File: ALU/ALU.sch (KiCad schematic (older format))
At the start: 40 parts, among them J1 Conn_01x16, J2 Conn_01x16, J3 Conn_01x08, J4 Conn_01x08, U1 74LS86, U10 74LS157, U11 74LS08, U12 74LS157, U13 74LS04, U2 74LS86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

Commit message: Fixed floating inputs; improved power; added parts list; replaced JK latches
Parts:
- added unit 4 of U11
- added unit 2 of U13
- added unit 3 of U13
- added unit 4 of U13
- added unit 5 of U13
- added unit 6 of U13
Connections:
- net GND: now also U13.11, U13.13, U13.3, U13.5, U13.9
- net VCC: now also U11.12, U11.13
- no-connect marks 0 -> 6
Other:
- moved on the sheet: U1E, U2E
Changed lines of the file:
@@
 	2150 5750 2250 5750
 Wire Wire Line
-	1300 7050 1300 7150
-Wire Wire Line
-	1300 5950 1300 6050
-Text GLabel 1300 5950 1    50   Input ~ 0
-VCC
-Text GLabel 1300 7150 3    50   Input ~ 0
+	1500 4950 1500 5050
+Wire Wire Line
+	1500 3850 1500 3950
+Text GLabel 1500 3850 1    50   Input ~ 0
+VCC
+Text GLabel 1500 5050 3    50   Input ~ 0
 GND
 $Comp
 L 74xx:74LS86 U2
 U 5 1 5FAF73A1
-P 1300 6550
-F 0 "U2" H 1530 6596 50  0000 L CNN
-F 1 "74LS86" H 1530 6505 50  0000 L CNN
-F 2 "Package_DIP:DIP-14_W7.62mm" H 1300 6550 50  0001 C CNN
-F 3 "74xx/74ls86.pdf" H 1300 6550 50  0001 C CNN
-	5    1300 6550
+P 1500 4450
+F 0 "U2" H 1650 4950 50  0000 L CNN
+F 1 "74LS86" H 1550 4850 50  0000 L CNN
+F 2 "Package_DIP:DIP-14_W7.62mm" H 1500 4450 50  0001 C CNN
+F 3 "74xx/74ls86.pdf" H 1500 4450 50  0001 C CNN
+	5    1500 4450
 	1    0    0    -1
 $EndComp
@@
 	2150 3250 2250 3250
 Wire Wire Line
-	1300 4500 1300 4600
-Wire Wire Line
-	1300 3400 1300 3500
-Text GLabel 1300 3400 1    50   Input ~ 0
-VCC
-Text GLabel 1300 4600 3    50   Input ~ 0
+	850  4950 850  5050
+Wire Wire Line
+	850  3850 850  3950
+Text GLabel 850  3850 1    50   Input ~ 0
+VCC
+Text GLabel 850  5050 3    50   Input ~ 0
 GND
 $Comp
 L 74xx:74LS86 U1
 U 5 1 5FA507DA
-P 1300 4000
-F 0 "U1" H 1530 4046 50  0000 L CNN
-F 1 "74LS86" H 1530 3955 50  0000 L CNN
-F 2 "Package_DIP:DIP-14_W7.62mm" H 1300 4000 50  0001 C CNN
-F 3 "74xx/74ls86.pdf" H 1300 4000 50  0001 C CNN
-	5    1300 4000
+P 850 4450
+F 0 "U1" H 1000 4950 50  0000 L CNN
+F 1 "74LS86" H 900 4850 50  0000 L CNN
+F 2 "Package_DIP:DIP-14_W7.62mm" H 850 4450 50  0001 C CNN
+F 3 "74xx/74ls86.pdf" H 850 4450 50  0001 C CNN
+	5    850  4450
 	1    0    0    -1
 $EndComp
@@
 Wire Wire Line
 	5200 6700 5200 6800
-Text GLabel 800  2750 1    50   Input ~ 0
+Text GLabel 850  2700 1    50   Input ~ 0
 VCC
 $Comp
 L power:PWR_FLAG #FLG0101
 U 1 1 5FC9E88A
-P 800 2800
-F 0 "#FLG0101" H 800 2875 50  0001 C CNN
-F 1 "PWR_FLAG" H 800 2973 50  0000 C CNN
-F 2 "" H 800 2800 50  0001 C CNN
-F 3 "~" H 800 2800 50  0001 C CNN
-	1    800  2800
+P 850 2750
+F 0 "#FLG0101" H 850 2825 50  0001 C CNN
+F 1 "PWR_FLAG" H 850 2923 50  0000 C CNN
+F 2 "" H 850 2750 50  0001 C CNN
+F 3 "~" H 850 2750 50  0001 C CNN
+	1    850  2750
 	-1   0    0    1
 $EndComp
 Wire Wire Line
-	800  2800 800  2750
-Wire Wire Line
-	800  3300 800  3350
+	850  2750 850  2700
+Wire Wire Line
+	850  3250 850  3300
 $Comp
 L power:PWR_FLAG #FLG0102
 U 1 1 5FCDF7DC
-P 800 3300
-F 0 "#FLG0102" H 800 3375 50  0001 C CNN
-F 1 "PWR_FLAG" H 800 3473 50  0000 C CNN
-F 2 "" H 800 3300 50  0001 C CNN
-F 3 "~" H 800 3300 50  0001 C CNN
-	1    800  3300
-	1    0    0    -1
-$EndComp
-Text GLabel 800  3350 3    50   Input ~ 0
+P 850 3250
+F 0 "#FLG0102" H 850 3325 50  0001 C CNN
+F 1 "PWR_FLAG" H 850 3423 50  0000 C CNN
+F 2 "" H 850 3250 50  0001 C CNN
+F 3 "~" H 850 3250 50  0001 C CNN
+	1    850  3250
+	1    0    0    -1
+$EndComp
+Text GLabel 850  3300 3    50   Input ~ 0
 GND
 $Comp
@@
 Wire Wire Line
 	9950 3350 10300 3350
+$Comp
+L 74xx:74LS04 U13
+U 4 1 60517929
+P 1250 6550
+F 0 "U13" H 1250 6867 50  0000 C CNN
+F 1 "74LS04" H 1250 6776 50  0000 C CNN
+F 2 "Package_DIP:DIP-14_W7.62mm" H 1250 6550 50  0001 C CNN
+F 3 "http://www.ti.com/lit/gpn/sn74LS04" H 1250 6550 50  0001 C CNN
+	4    1250 6550
+	1    0    0    -1
+$EndComp
+$Comp
+L 74xx:74LS04 U13
+U 5 1 6051A436
+P 1250 7050
+F 0 "U13" H 1250 7367 50  0000 C CNN
+F 1 "74LS04" H 1250 7276 50  0000 C CNN
+F 2 "Package_DIP:DIP-14_W7.62mm" H 1250 7050 50  0001 C CNN
+F 3 "http://www.ti.com/lit/gpn/sn74LS04" H 1250 7050 50  0001 C CNN
+	5    1250 7050
+	1    0    0    -1
+$EndComp
+$Comp
+L 74xx:74LS04 U13
+U 6 1 6051C4D5
+P 1250 7550
+F 0 "U13" H 1250 7867 50  0000 C CNN
+F 1 "74LS04" H 1250 7776 50  0000 C CNN
+F 2 "Package_DIP:DIP-14_W7.62mm" H 1250 7550 50  0001 C CNN
+F 3 "http://www.ti.com/lit/gpn/sn74LS04" H 1250 7550 50  0001 C CNN
+	6    1250 7550
+	1    0    0    -1
+$EndComp
+$Comp
+L 74xx:74LS08 U11
+U 4 1 6050CEA2
+P 6350 7100
+F 0 "U11" H 6350 7425 50  0000 C CNN
+F 1 "74LS08" H 6350 7334 50  0000 C CNN
+F 2 "Package_DIP:DIP-14_W7.62mm" H 6350 7100 50  0001 C CNN
+F 3 "http://www.ti.com/lit/gpn/sn74LS08" H 6350 7100 50  0001 C CNN
+	4    6350 7100
+	1    0    0    -1
+$EndComp
+$Comp
+L 74xx:74LS04 U13
+U 3 1 60514840
+P 1250 6050
+F 0 "U13" H 1250 6367 50  0000 C CNN
+F 1 "74LS04" H 1250 6276 50  0000 C CNN
+F 2 "Package_DIP:DIP-14_W7.62mm" H 1250 6050 50  0001 C CNN
+F 3 "http://www.ti.com/lit/gpn/sn74LS04" H 1250 6050 50  0001 C CNN
+	3    1250 6050
+	1    0    0    -1
+$EndComp
+$Comp
+L 74xx:74LS04 U13
+U 2 1 60510F55
+P 1250 5550
+F 0 "U13" H 1250 5867 50  0000 C CNN
+F 1 "74LS04" H 1250 5776 50  0000 C CNN
+F 2 "Package_DIP:DIP-14_W7.62mm" H 1250 5550 50  0001 C CNN
+F 3 "http://www.ti.com/lit/gpn/sn74LS04" H 1250 5550 50  0001 C CNN
+	2    1250 5550
+	1    0    0    -1
+$EndComp
+Text GLabel 850  5550 0    50   Input ~ 0
+GND
+Wire Wire Line
+	850  5550 950  5550
+Text GLabel 850  6050 0    50   Input ~ 0
+GND
+Wire Wire Line
+	850  6050 950  6050
+Text GLabel 850  6550 0    50   Input ~ 0
+GND
+Wire Wire Line
+	850  6550 950  6550
+Text GLabel 850  7050 0    50   Input ~ 0
+GND
+Wire Wire Line
+	850  7050 950  7050
+Text GLabel 850  7550 0    50   Input ~ 0
+GND
+Wire Wire Line
+	850  7550 950  7550
+NoConn ~ 1550 5550
+NoConn ~ 1550 6050
+NoConn ~ 1550 6550
+NoConn ~ 1550 7050
+NoConn ~ 1550 7550
+Text GLabel 5950 7100 0    50   Input ~ 0
+VCC
+Wire Wire Line
+	6050 7000 6050 7100
+Wire Wire Line
+	5950 7100 6050 7100
+Connection ~ 6050 7100
+Wire Wire Line
+	6050 7100 6050 7200
+NoConn ~ 6650 7100
 $EndSCHEMATC

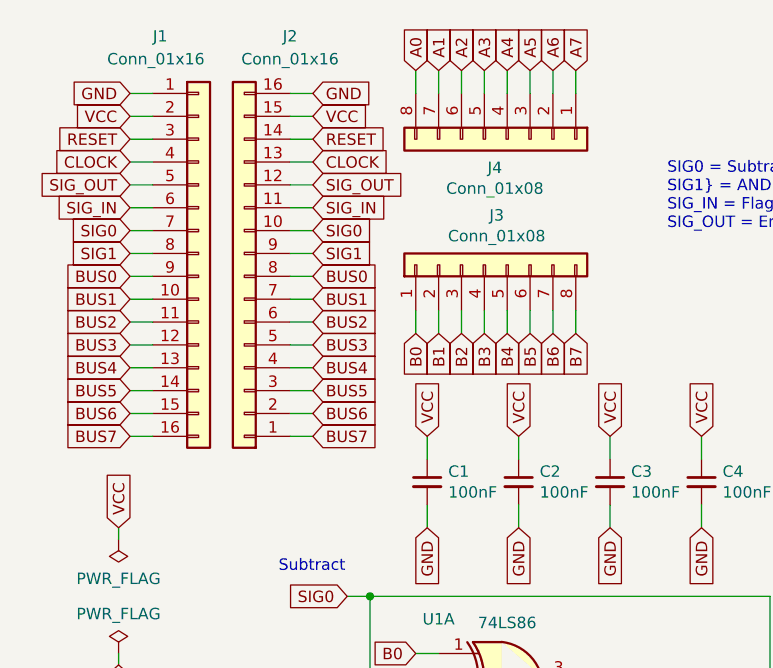
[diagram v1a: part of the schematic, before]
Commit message: Fix reversed headers on ALU, and counting issues on counter (CET / CEP connections)
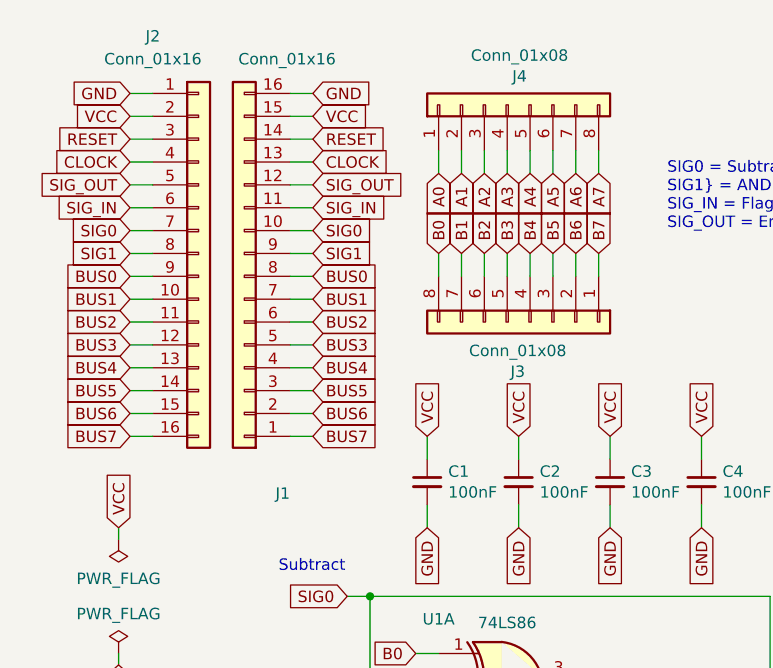
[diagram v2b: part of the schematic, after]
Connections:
- net A0: now also J4.1 (Pin_1); no longer J4.8 (Pin_8)
- net A1: now also J4.2 (Pin_2); no longer J4.7 (Pin_7)
- net A2: now also J4.3 (Pin_3); no longer J4.6 (Pin_6)
- net A3: now also J4.4 (Pin_4); no longer J4.5 (Pin_5)
- net A4: now also J4.5 (Pin_5); no longer J4.4 (Pin_4)
- net A5: now also J4.6 (Pin_6); no longer J4.3 (Pin_3)
- net A6: now also J4.7 (Pin_7); no longer J4.2 (Pin_2)
- net A7: now also J4.8 (Pin_8); no longer J4.1 (Pin_1)
- net B0: now also J3.8 (Pin_8); no longer J3.1 (Pin_1)
- net B1: now also J3.7 (Pin_7); no longer J3.2 (Pin_2)
- net B2: now also J3.6 (Pin_6); no longer J3.3 (Pin_3)
- net B3: now also J3.5 (Pin_5); no longer J3.4 (Pin_4)
- net B4: now also J3.4 (Pin_4); no longer J3.5 (Pin_5)
- net B5: now also J3.3 (Pin_3); no longer J3.6 (Pin_6)
- net B6: now also J3.2 (Pin_2); no longer J3.7 (Pin_7)
- net B7: now also J3.1 (Pin_1); no longer J3.8 (Pin_8)
- net BUS0: now also J1.8 (Pin_8), J2.9 (Pin_9); no longer J1.9 (Pin_9), J2.8 (Pin_8)
- net BUS1: now also J1.7 (Pin_7), J2.10 (Pin_10); no longer J1.10 (Pin_10), J2.7 (Pin_7)
- net BUS2: now also J1.6 (Pin_6), J2.11 (Pin_11); no longer J1.11 (Pin_11), J2.6 (Pin_6)
- net BUS3: now also J1.5 (Pin_5), J2.12 (Pin_12); no longer J1.12 (Pin_12), J2.5 (Pin_5)
- net BUS4: now also J1.4 (Pin_4), J2.13 (Pin_13); no longer J1.13 (Pin_13), J2.4 (Pin_4)
- net BUS5: now also J1.3 (Pin_3), J2.14 (Pin_14); no longer J1.14 (Pin_14), J2.3 (Pin_3)
- net BUS6: now also J1.2 (Pin_2), J2.15 (Pin_15); no longer J1.15 (Pin_15), J2.2 (Pin_2)
- net BUS7: now also J1.1 (Pin_1), J2.16 (Pin_16); no longer J1.16 (Pin_16), J2.1 (Pin_1)
- net CLOCK: now also J1.13 (Pin_13), J2.4 (Pin_4); no longer J1.4 (Pin_4), J2.13 (Pin_13)
- net GND: now also J1.16 (Pin_16), J2.1 (Pin_1); no longer J1.1 (Pin_1), J2.16 (Pin_16)
- net RESET: now also J1.14 (Pin_14), J2.3 (Pin_3); no longer J1.3 (Pin_3), J2.14 (Pin_14)
- net SIG0: now also J1.10 (Pin_10), J2.7 (Pin_7); no longer J1.7 (Pin_7), J2.10 (Pin_10)
- net SIG1: now also J1.9 (Pin_9), J2.8 (Pin_8); no longer J1.8 (Pin_8), J2.9 (Pin_9)
- net SIG_IN: now also J1.11 (Pin_11), J2.6 (Pin_6); no longer J1.6 (Pin_6), J2.11 (Pin_11)
- net SIG_OUT: now also J1.12 (Pin_12), J2.5 (Pin_5); no longer J1.5 (Pin_5), J2.12 (Pin_12)
- net VCC: now also J1.15 (Pin_15), J2.2 (Pin_2); no longer J1.2 (Pin_2), J2.15 (Pin_15)
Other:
- moved on the sheet: J1, J2, J3, J4
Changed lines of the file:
@@
 $EndDescr
 $Comp
-L Connector_Generic:Conn_01x16 J1
-U 1 1 5F957F2C
+L Connector_Generic:Conn_01x16 J2
+U 1 1 5F9602A3
 P 1200 1500
-F 0 "J1" H 1000 2450 50  0000 L CNN
-F 1 "Conn_01x16" H 800 2350 50  0000 L CNN
+F 0 "J2" H 1000 2450 50  0000 C CNN
+F 1 "Conn_01x16" H 1000 2350 50  0000 C CNN
 F 2 "Connector_PinHeader_2.54mm:PinHeader_1x16_P2.54mm_Horizontal" H 1200 1500 50  0001 C CNN
 F 3 "~" H 1200 1500 50  0001 C CNN
 	1    1200 1500
 	1    0    0    -1
-$EndComp
-$Comp
-L Connector_Generic:Conn_01x16 J2
-U 1 1 5F9602A3
-P 1400 1600
-F 0 "J2" H 1200 550 50  0000 C CNN
-F 1 "Conn_01x16" H 1200 650 50  0000 C CNN
-F 2 "Connector_PinHeader_2.54mm:PinHeader_1x16_P2.54mm_Horizontal" H 1400 1600 50  0001 C CNN
-F 3 "~" H 1400 1600 50  0001 C CNN
-	1    1400 1600
-	-1   0    0    1
 $EndComp
 Text GLabel 900  900  0    50   Input ~ 0
@@
 Wire Wire Line
 	1700 1000 1600 1000
-$Comp
-L Connector_Generic:Conn_01x08 J4
-U 1 1 5F96CACD
-P 2550 1000
-F 0 "J4" V 2675 946 50  0000 C CNN
-F 1 "Conn_01x08" V 2766 946 50  0000 C CNN
-F 2 "Connector_PinHeader_2.54mm:PinHeader_1x08_P2.54mm_Horizontal" H 2550 1000 50  0001 C CNN
-F 3 "~" H 2550 1000 50  0001 C CNN
-	1    2550 1000
-	0    1    1    0
-$EndComp
-$Comp
-L Connector_Generic:Conn_01x08 J3
-U 1 1 5F96EEC7
-P 2450 1550
-F 0 "J3" V 2667 1496 50  0000 C CNN
-F 1 "Conn_01x08" V 2576 1496 50  0000 C CNN
-F 2 "Connector_PinHeader_2.54mm:PinHeader_1x08_P2.54mm_Horizontal" H 2450 1550 50  0001 C CNN
-F 3 "~" H 2450 1550 50  0001 C CNN
-	1    2450 1550
-	0    -1   -1   0
-$EndComp
-Text GLabel 2250 700  1    50   Input ~ 0
+Text GLabel 2350 1150 3    50   Input ~ 0
 A1
-Text GLabel 2350 700  1    50   Input ~ 0
+Text GLabel 2450 1150 3    50   Input ~ 0
 A2
-Text GLabel 2550 700  1    50   Input ~ 0
+Text GLabel 2650 1150 3    50   Input ~ 0
 A4
-Text GLabel 2650 700  1    50   Input ~ 0
+Text GLabel 2750 1150 3    50   Input ~ 0
 A5
-Text GLabel 2750 700  1    50   Input ~ 0
+Text GLabel 2850 1150 3    50   Input ~ 0
 A6
-Text GLabel 2850 700  1    50   Input ~ 0
+Text GLabel 2950 1150 3    50   Input ~ 0
 A7
-Text GLabel 2150 700  1    50   Input ~ 0
-A0
-Wire Wire Line
-	2150 800  2150 700
-Wire Wire Line
-	2250 800  2250 700
-Wire Wire Line
-	2350 800  2350 700
-Wire Wire Line
-	2450 800  2450 700
-Wire Wire Line
-	2550 800  2550 700
-Wire Wire Line
-	2650 800  2650 700
-Wire Wire Line
-	2750 800  2750 700
-Wire Wire Line
-	2850 800  2850 700
-Wire Wire Line
-	2150 1850 2150 1750
-Wire Wire Line
-	2250 1850 2250 1750
-Wire Wire Line
-	2350 1850 2350 1750
-Wire Wire Line
-	2450 1850 2450 1750
-Wire Wire Line
-	2550 1850 2550 1750
-Wire Wire Line
-	2650 1850 2650 1750
-Wire Wire Line
-	2750 1850 2750 1750
-Wire Wire Line
-	2850 1850 2850 1750
-Text GLabel 2150 1850 3    50   Input ~ 0
+Wire Wire Line
+	2250 1600 2250 1500
+Wire Wire Line
+	2350 1600 2350 1500
+Wire Wire Line
+	2450 1600 2450 1500
+Wire Wire Line
+	2550 1600 2550 1500
+Wire Wire Line
+	2650 1600 2650 1500
+Wire Wire Line
+	2750 1600 2750 1500
+Wire Wire Line
+	2850 1600 2850 1500
+Wire Wire Line
+	2950 1600 2950 1500
+Wire Wire Line
+	2250 1150 2250 1050
+Wire Wire Line
+	2350 1150 2350 1050
+Wire Wire Line
+	2450 1150 2450 1050
+Wire Wire Line
+	2550 1150 2550 1050
+Wire Wire Line
+	2650 1150 2650 1050
+Wire Wire Line
+	2750 1150 2750 1050
+Wire Wire Line
+	2850 1150 2850 1050
+Wire Wire Line
+	2950 1150 2950 1050
+Text GLabel 2250 1500 1    50   Input ~ 0
 B0
-Text GLabel 2250 1850 3    50   Input ~ 0
+Text GLabel 2350 1500 1    50   Input ~ 0
 B1
-Text GLabel 2350 1850 3    50   Input ~ 0
+Text GLabel 2450 1500 1    50   Input ~ 0
 B2
-Text GLabel 2450 700  1    50   Input ~ 0
+Text GLabel 2550 1150 3    50   Input ~ 0
 A3
-Text GLabel 2450 1850 3    50   Input ~ 0
+Text GLabel 2550 1500 1    50   Input ~ 0
 B3
-Text GLabel 2550 1850 3    50   Input ~ 0
+Text GLabel 2650 1500 1    50   Input ~ 0
 B4
-Text GLabel 2750 1850 3    50   Input ~ 0
+Text GLabel 2850 1500 1    50   Input ~ 0
 B6
-Text GLabel 2850 1850 3    50   Input ~ 0
+Text GLabel 2950 1500 1    50   Input ~ 0
 B7
-Text GLabel 2650 1850 3    50   Input ~ 0
+Text GLabel 2750 1500 1    50   Input ~ 0
 B5
 Wire Wire Line
@@
 	6050 7100 6050 7200
 NoConn ~ 6650 7100
+Text GLabel 2250 1150 3    50   Input ~ 0
+A0
+$Comp
+L Connector_Generic:Conn_01x08 J3
+U 1 1 5F96EEC7
+P 2650 1800
+F 0 "J3" V 2867 1746 50  0000 C CNN
+F 1 "Conn_01x08" V 2776 1746 50  0000 C CNN
+F 2 "Connector_PinHeader_2.54mm:PinHeader_1x08_P2.54mm_Horizontal" H 2650 1800 50  0001 C CNN
+F 3 "~" H 2650 1800 50  0001 C CNN
+	1    2650 1800
+	0    1    1    0
+$EndComp
+$Comp
+L Connector_Generic:Conn_01x08 J4
+U 1 1 5F96CACD
+P 2550 850
+F 0 "J4" V 2675 796 50  0000 C CNN
+F 1 "Conn_01x08" V 2766 796 50  0000 C CNN
+F 2 "Connector_PinHeader_2.54mm:PinHeader_1x08_P2.54mm_Horizontal" H 2550 850 50  0001 C CNN
+F 3 "~" H 2550 850 50  0001 C CNN
+	1    2550 850
+	0    -1   -1   0
+$EndComp
+$Comp
+L Connector_Generic:Conn_01x16 J1
+U 1 1 5F957F2C
+P 1400 1600
+F 0 "J1" H 1200 2550 50  0000 L CNN
+F 1 "Conn_01x16" H 1000 650 50  0000 L CNN
+F 2 "Connector_PinHeader_2.54mm:PinHeader_1x16_P2.54mm_Horizontal" H 1400 1600 50  0001 C CNN
+F 3 "~" H 1400 1600 50  0001 C CNN
+	1    1400 1600
+	-1   0    0    1
+$EndComp
 $EndSCHEMATC

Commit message: Update all boards to r3, and update revision log and gitignore
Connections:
- net at U12.4 (Za), U9.2 (A0): now also D8.2 (A); no longer D1.2 (A)
- net at U12.7 (Zb), U9.3 (A1): now also D7.2 (A); no longer D2.2 (A)
- net at U12.9 (Zc), U9.4 (A2): now also D6.2 (A); no longer D3.2 (A)
- net at U12.12 (Zd), U9.5 (A3): now also D5.2 (A); no longer D4.2 (A)
- net at U10.4 (Za), U7.8, U9.6 (A4): now also D4.2 (A); no longer D5.2 (A)
- net at U10.7 (Zb), U7.9, U9.7 (A5): now also D3.2 (A); no longer D6.2 (A)
- net at U10.9 (Zc), U7.11, U9.8 (A6): now also D2.2 (A); no longer D7.2 (A)
- net at U10.12 (Zd), U7.12, U9.9 (A7): now also D1.2 (A); no longer D8.2 (A)
- net at D1.1 (K): now also RN1.9 (R8); no longer RN1.2 (R1)
- net at D2.1 (K): now also RN1.8 (R7); no longer RN1.3 (R2)
- net at D3.1 (K): now also RN1.7 (R6); no longer RN1.4 (R3)
- net at D4.1 (K): now also RN1.6 (R5); no longer RN1.5 (R4)
- net at D5.1 (K): now also RN1.5 (R4); no longer RN1.6 (R5)
- net at D6.1 (K): now also RN1.4 (R3); no longer RN1.7 (R6)
- net at D7.1 (K): now also RN1.3 (R2); no longer RN1.8 (R7)
- net at D8.1 (K): now also RN1.2 (R1); no longer RN1.9 (R8)
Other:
- moved on the sheet: D1, D2, D3, D4, D5, D6, D7, D8
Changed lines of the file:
@@
 L Device:LED_Small_ALT D1
 U 1 1 5FA8CEA3
-P 10400 3350
-F 0 "D1" V 10446 3282 50  0000 R CNN
-F 1 "LED" V 10355 3282 50  0000 R CNN
-F 2 "LED_THT:LED_D3.0mm_Clear" V 10400 3350 50  0001 C CNN
-F 3 "~" V 10400 3350 50  0001 C CNN
-	1    10400 3350
+P 10400 4400
+F 0 "D1" V 10446 4332 50  0000 R CNN
+F 1 "LED" V 10355 4332 50  0000 R CNN
+F 2 "LED_THT:LED_D3.0mm_Clear" V 10400 4400 50  0001 C CNN
+F 3 "~" V 10400 4400 50  0001 C CNN
+	1    10400 4400
 	-1   0    0    1
 $EndComp
@@
 L Device:LED_Small_ALT D2
 U 1 1 5FA9128B
+P 10400 4250
+F 0 "D2" V 10446 4182 50  0000 R CNN
+F 1 "LED" V 10355 4182 50  0000 R CNN
+F 2 "LED_THT:LED_D3.0mm_Clear" V 10400 4250 50  0001 C CNN
+F 3 "~" V 10400 4250 50  0001 C CNN
+	1    10400 4250
+	-1   0    0    1
+$EndComp
+$Comp
+L Device:LED_Small_ALT D3
+U 1 1 5FA9DF77
+P 10400 4100
+F 0 "D3" V 10446 4032 50  0000 R CNN
+F 1 "LED" V 10355 4032 50  0000 R CNN
+F 2 "LED_THT:LED_D3.0mm_Clear" V 10400 4100 50  0001 C CNN
+F 3 "~" V 10400 4100 50  0001 C CNN
+	1    10400 4100
+	-1   0    0    1
+$EndComp
+$Comp
+L Device:LED_Small_ALT D4
+U 1 1 5FAAAACD
+P 10400 3950
+F 0 "D4" V 10446 3882 50  0000 R CNN
+F 1 "LED" V 10355 3882 50  0000 R CNN
+F 2 "LED_THT:LED_D3.0mm_Clear" V 10400 3950 50  0001 C CNN
+F 3 "~" V 10400 3950 50  0001 C CNN
+	1    10400 3950
+	-1   0    0    1
+$EndComp
+$Comp
+L Device:LED_Small_ALT D5
+U 1 1 5FAB9D8B
+P 10400 3800
+F 0 "D5" V 10446 3732 50  0000 R CNN
+F 1 "LED" V 10355 3732 50  0000 R CNN
+F 2 "LED_THT:LED_D3.0mm_Clear" V 10400 3800 50  0001 C CNN
+F 3 "~" V 10400 3800 50  0001 C CNN
+	1    10400 3800
+	-1   0    0    1
+$EndComp
+$Comp
+L Device:LED_Small_ALT D6
+U 1 1 5FAB9D91
+P 10400 3650
+F 0 "D6" V 10446 3582 50  0000 R CNN
+F 1 "LED" V 10355 3582 50  0000 R CNN
+F 2 "LED_THT:LED_D3.0mm_Clear" V 10400 3650 50  0001 C CNN
+F 3 "~" V 10400 3650 50  0001 C CNN
+	1    10400 3650
+	-1   0    0    1
+$EndComp
+$Comp
+L Device:LED_Small_ALT D7
+U 1 1 5FAB9D97
 P 10400 3500
-F 0 "D2" V 10446 3432 50  0000 R CNN
+F 0 "D7" V 10446 3432 50  0000 R CNN
 F 1 "LED" V 10355 3432 50  0000 R CNN
 F 2 "LED_THT:LED_D3.0mm_Clear" V 10400 3500 50  0001 C CNN
@@
 $EndComp
 $Comp
-L Device:LED_Small_ALT D3
-U 1 1 5FA9DF77
-P 10400 3650
-F 0 "D3" V 10446 3582 50  0000 R CNN
-F 1 "LED" V 10355 3582 50  0000 R CNN
-F 2 "LED_THT:LED_D3.0mm_Clear" V 10400 3650 50  0001 C CNN
-F 3 "~" V 10400 3650 50  0001 C CNN
-	1    10400 3650
+L Device:LED_Small_ALT D8
+U 1 1 5FAB9D9D
+P 10400 3350
+F 0 "D8" V 10446 3282 50  0000 R CNN
+F 1 "LED" V 10355 3282 50  0000 R CNN
+F 2 "LED_THT:LED_D3.0mm_Clear" V 10400 3350 50  0001 C CNN
+F 3 "~" V 10400 3350 50  0001 C CNN
+	1    10400 3350
 	-1   0    0    1
 $EndComp
-$Comp
-L Device:LED_Small_ALT D4
-U 1 1 5FAAAACD
-P 10400 3800
-F 0 "D4" V 10446 3732 50  0000 R CNN
-F 1 "LED" V 10355 3732 50  0000 R CNN
-F 2 "LED_THT:LED_D3.0mm_Clear" V 10400 3800 50  0001 C CNN
-F 3 "~" V 10400 3800 50  0001 C CNN
-	1    10400 3800
-	-1   0    0    1
-$EndComp
-$Comp
-L Device:LED_Small_ALT D5
-U 1 1 5FAB9D8B
-P 10400 3950
-F 0 "D5" V 10446 3882 50  0000 R CNN
-F 1 "LED" V 10355 3882 50  0000 R CNN
-F 2 "LED_THT:LED_D3.0mm_Clear" V 10400 3950 50  0001 C CNN
-F 3 "~" V 10400 3950 50  0001 C CNN
-	1    10400 3950
-	-1   0    0    1
-$EndComp
-$Comp
-L Device:LED_Small_ALT D6
-U 1 1 5FAB9D91
-P 10400 4100
-F 0 "D6" V 10446 4032 50  0000 R CNN
-F 1 "LED" V 10355 4032 50  0000 R CNN
-F 2 "LED_THT:LED_D3.0mm_Clear" V 10400 4100 50  0001 C CNN
-F 3 "~" V 10400 4100 50  0001 C CNN
-	1    10400 4100
-	-1   0    0    1
-$EndComp
-$Comp
-L Device:LED_Small_ALT D7
-U 1 1 5FAB9D97
-P 10400 4250
-F 0 "D7" V 10446 4182 50  0000 R CNN
-F 1 "LED" V 10355 4182 50  0000 R CNN
-F 2 "LED_THT:LED_D3.0mm_Clear" V 10400 4250 50  0001 C CNN
-F 3 "~" V 10400 4250 50  0001 C CNN
-	1    10400 4250
-	-1   0    0    1
-$EndComp
-$Comp
-L Device:LED_Small_ALT D8
-U 1 1 5FAB9D9D
-P 10400 4400
-F 0 "D8" V 10446 4332 50  0000 R CNN
-F 1 "LED" V 10355 4332 50  0000 R CNN
-F 2 "LED_THT:LED_D3.0mm_Clear" V 10400 4400 50  0001 C CNN
-F 3 "~" V 10400 4400 50  0001 C CNN
-	1    10400 4400
-	-1   0    0    1
-$EndComp
